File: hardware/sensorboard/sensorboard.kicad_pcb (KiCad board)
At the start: 2 copper layers, 51.7 x 19.3 mm, 23 parts, among them P1 PWR, P2 PROG, U1 ESP-07v2, U2 LMR16006Y, U3 BMP180_board, U4 DHT22

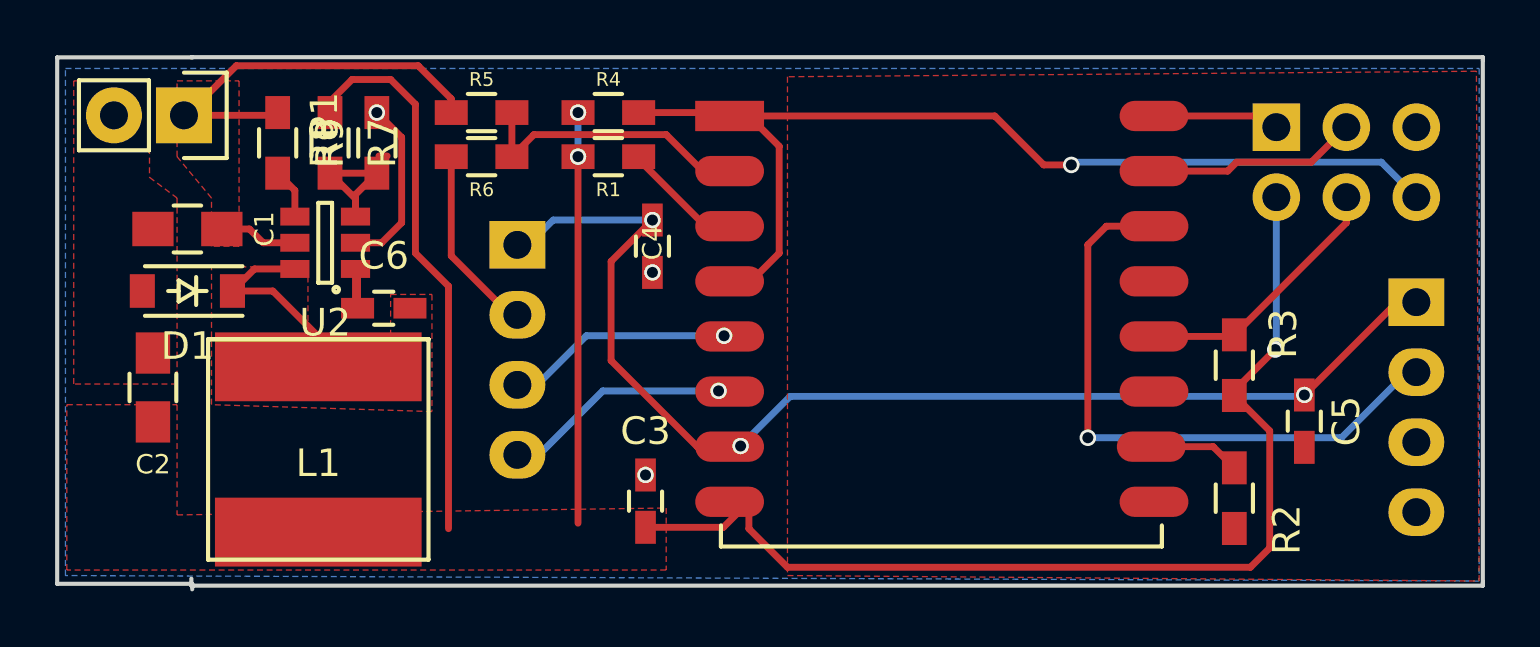
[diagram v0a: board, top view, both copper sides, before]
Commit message: Fix up silkscreening
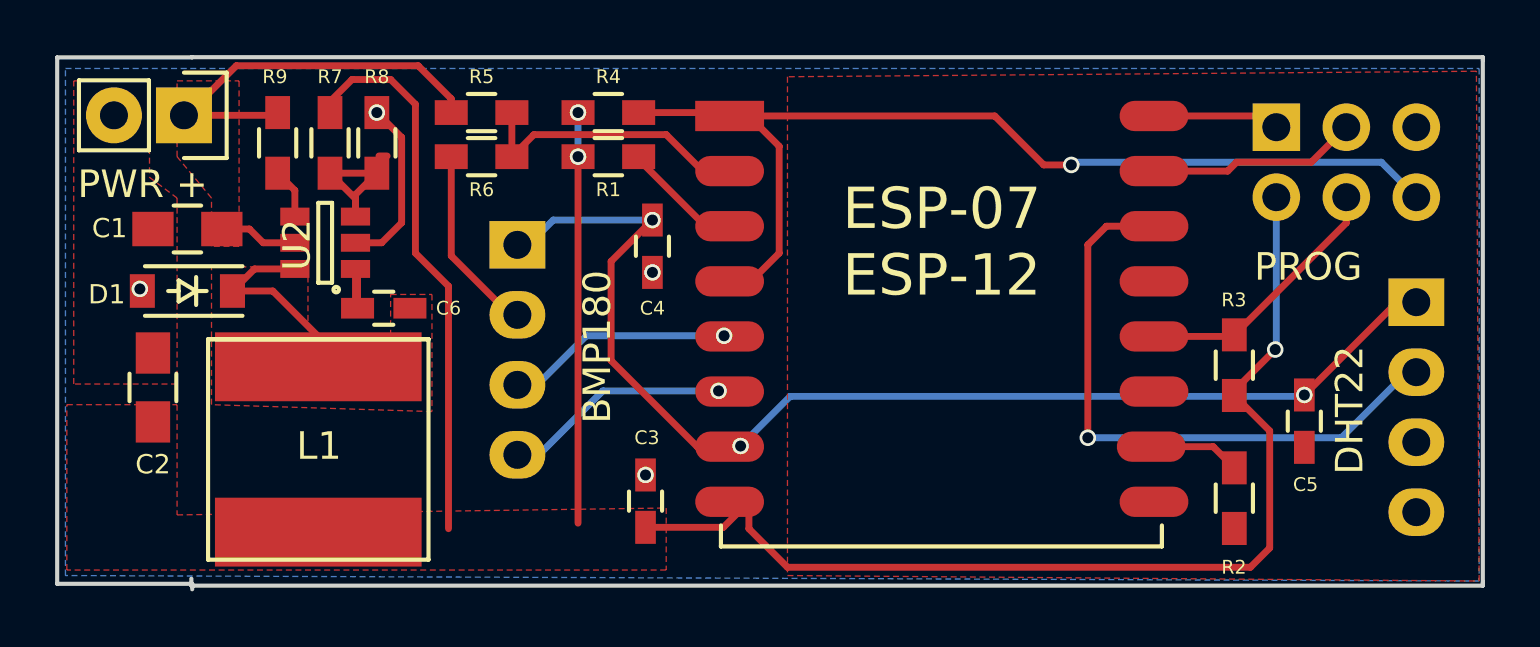
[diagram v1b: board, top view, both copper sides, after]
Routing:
- net GND: track 13.7 -> 13.8 mm, vias 3 -> 4
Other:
- board text added: "BMP180"
- board text added: "DATA"
- board text added: "DHT22"
- board text added: "ESP sensorboard v3.0"
- board text added: "ESP-07 ESP-12"
- board text added: "GND"
- board text added: "PROG"
- board text added: "PWR +"
- board text added: "SCL"
- board text added: "SDA"
- board text added: "VIN"
- board text added: "z2amiller"
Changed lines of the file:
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@@
     (area 123.324999 72.314999 175.208001 91.775001)
     (thickness 1.6)
-    (drawings 10)
-    (tracks 130)
+    (drawings 24)
+    (tracks 132)
     (zones 0)
     (modules 23)
@@
     (visible_elements FFFEFF7F)
     (pcbplotparams
-      (layerselection 0x010f0_80000001)
+      (layerselection 0x010f0_ffffffff)
       (usegerberextensions true)
       (excludeedgelayer true)
@@
     (tags "capacitor 0805")
     (attr smd)
-    (fp_text reference C1 (at -2.794 0 270) (layer F.SilkS)
+    (fp_text reference C1 (at 2.825 0.025 360) (layer F.SilkS)
       (effects (font (size 0.7 0.7) (thickness 0.1)))
     )
@@
     (attr smd)
     (fp_text reference C2 (at -2.794 0 180) (layer F.SilkS)
-      (effects (font (size 0.7 0.7) (thickness 0.15)))
+      (effects (font (size 0.7 0.7) (thickness 0.1)))
     )
     (fp_text value 10uf (at 0 2.1 90) (layer F.Fab)
@@
     (tags "resistor 0603")
     (attr smd)
-    (fp_text reference R4 (at 0 -1.2) (layer F.SilkS)
-      (effects (font (size 0.5 0.5) (thickness 0.125)))
+    (fp_text reference R4 (at 0 -1.3) (layer F.SilkS)
+      (effects (font (size 0.5 0.5) (thickness 0.1)))
     )
     (fp_text value 10k (at 0 1.9) (layer F.Fab)
@@
     (tags "resistor 0603")
     (attr smd)
-    (fp_text reference R3 (at 1.143 1.778 270) (layer F.SilkS)
-      (effects (font (size 1 1) (thickness 0.15)))
+    (fp_text reference R3 (at 2.366 -0.016 180) (layer F.SilkS)
+      (effects (font (size 0.5 0.5) (thickness 0.1)))
     )
     (fp_text value 10k (at 0 1.9 90) (layer F.Fab)
@@
     (tags "resistor 0603")
     (attr smd)
-    (fp_text reference R2 (at 1.143 -1.905 450) (layer F.SilkS)
-      (effects (font (size 1 1) (thickness 0.15)))
+    (fp_text reference R2 (at 2.508 0.016 360) (layer F.SilkS)
+      (effects (font (size 0.5 0.5) (thickness 0.1)))
     )
     (fp_text value 10k (at 0 1.9 270) (layer F.Fab)
@@
     (attr smd)
     (fp_text reference R1 (at 0 1.2) (layer F.SilkS)
-      (effects (font (size 0.5 0.5) (thickness 0.125)))
+      (effects (font (size 0.5 0.5) (thickness 0.1)))
     )
     (fp_text value 10k (at 0 1.9) (layer F.Fab)
@@
     (tags "capacitor 0603")
     (attr smd)
-    (fp_text reference C5 (at 0 1.524 90) (layer F.SilkS)
-      (effects (font (size 1 1) (thickness 0.15)))
+    (fp_text reference C5 (at -2.302 0.044 180) (layer F.SilkS)
+      (effects (font (size 0.5 0.5) (thickness 0.1)))
     )
     (fp_text value 100nf (at 0 1.9 90) (layer F.Fab)
@@
     (tags "capacitor 0603")
     (attr smd)
-    (fp_text reference C3 (at 2.54 0 180) (layer F.SilkS)
-      (effects (font (size 1 1) (thickness 0.15)))
+    (fp_text reference C3 (at 2.3 0.05 180) (layer F.SilkS)
+      (effects (font (size 0.5 0.5) (thickness 0.1)))
     )
     (fp_text value 100nf (at 0 1.9 90) (layer F.Fab)
@@
     (tags "capacitor 0603")
     (attr smd)
-    (fp_text reference C4 (at 0.127 0 90) (layer F.SilkS)
-      (effects (font (size 0.7 0.7) (thickness 0.15)))
+    (fp_text reference C4 (at -2.25 0 180) (layer F.SilkS)
+      (effects (font (size 0.5 0.5) (thickness 0.1)))
     )
     (fp_text value 100nf (at 0 1.9 90) (layer F.Fab)
@@
     (tags "resistor 0603")
     (attr smd)
-    (fp_text reference R5 (at 0 -1.2) (layer F.SilkS)
-      (effects (font (size 0.5 0.5) (thickness 0.125)))
+    (fp_text reference R5 (at 0 -1.3) (layer F.SilkS)
+      (effects (font (size 0.5 0.5) (thickness 0.1)))
     )
     (fp_text value 470K (at 0 1.9) (layer F.Fab)
@@
     (attr smd)
     (fp_text reference R6 (at 0 -1.2 180) (layer F.SilkS)
-      (effects (font (size 0.5 0.5) (thickness 0.125)))
+      (effects (font (size 0.5 0.5) (thickness 0.1)))
     )
     (fp_text value 47K (at 0 1.9 180) (layer F.Fab)
@@
     (tags "capacitor 0603")
     (attr smd)
-    (fp_text reference C6 (at 0 -1.9) (layer F.SilkS)
-      (effects (font (size 1 1) (thickness 0.15)))
+    (fp_text reference C6 (at 2.35 0) (layer F.SilkS)
+      (effects (font (size 0.5 0.5) (thickness 0.1)))
     )
     (fp_text value 1uf (at 0 1.9) (layer F.Fab)
@@
     (tags SOD-123)
     (attr smd)
-    (fp_text reference D1 (at 0 -2 180) (layer F.SilkS)
-      (effects (font (size 1 1) (thickness 0.15)))
+    (fp_text reference D1 (at 2.925 -0.125 180) (layer F.SilkS)
+      (effects (font (size 0.7 0.7) (thickness 0.1)))
     )
     (fp_text value "60V 1A" (at 0 2.1 180) (layer F.Fab)
@@
   (module Inductors:NR8040_HandSoldering (layer F.Cu)
     (at 132.875 86.625)
-    (fp_text reference L1 (at 0 0.5) (layer F.SilkS)
+    (fp_text reference L1 (at 0.025 -0.125) (layer F.SilkS)
       (effects (font (size 1 1) (thickness 0.15)))
     )
@@
     (descr "Through hole pin header")
     (tags "pin header")
-    (fp_text reference P1 (at 0 -5.1 270) (layer F.SilkS)
+    (fp_text reference P1 (at 2.5 2.5 360) (layer F.SilkS) hide
       (effects (font (size 1 1) (thickness 0.15)))
     )
@@
     (tags "resistor 0603")
     (attr smd)
-    (fp_text reference R7 (at 0 -1.9 270) (layer F.SilkS)
-      (effects (font (size 1 1) (thickness 0.15)))
+    (fp_text reference R7 (at -2.4 0 360) (layer F.SilkS)
+      (effects (font (size 0.5 0.5) (thickness 0.1)))
     )
     (fp_text value 33k (at 0 1.9 270) (layer F.Fab)
@@
     (tags "resistor 0603")
     (attr smd)
-    (fp_text reference R8 (at 0 -1.9 90) (layer F.SilkS)
-      (effects (font (size 1 1) (thickness 0.15)))
+    (fp_text reference R8 (at 2.4 0 180) (layer F.SilkS)
+      (effects (font (size 0.5 0.5) (thickness 0.1)))
     )
     (fp_text value 10k (at 0 1.9 90) (layer F.Fab)
@@
     (tags "resistor 0603")
     (attr smd)
-    (fp_text reference R9 (at 0 -1.9 270) (layer F.SilkS)
-      (effects (font (size 1 1) (thickness 0.15)))
+    (fp_text reference R9 (at -2.4 0.1 360) (layer F.SilkS)
+      (effects (font (size 0.5 0.5) (thickness 0.1)))
     )
     (fp_text value 100k (at 0 1.9 270) (layer F.Fab)
@@
     (tags SOT-23-6)
     (attr smd)
-    (fp_text reference U2 (at 0 -2.9 180) (layer F.SilkS)
+    (fp_text reference U2 (at 1.025 -0.075 450) (layer F.SilkS)
       (effects (font (size 1 1) (thickness 0.15)))
     )
@@
       (rotate (xyz 0 0 0))
     )
+  )
+  (gr_text SDA (at 143 86.8) (layer B.SilkS)
+    (effects (font (size 0.7 0.7) (thickness 0.15)) (justify mirror))
+  )
+  (gr_text SCL (at 142.9 84.3) (layer B.SilkS)
+    (effects (font (size 0.7 0.7) (thickness 0.15)) (justify mirror))
+  )
+  (gr_text VIN (at 142.8 79.2) (layer B.SilkS)
+    (effects (font (size 0.7 0.7) (thickness 0.15)) (justify mirror))
+  )
+  (gr_text GND (at 142.9 81.8) (layer B.SilkS)
+    (effects (font (size 0.7 0.7) (thickness 0.15)) (justify mirror))
+  )
+  (gr_text GND (at 169.9 89) (layer B.SilkS)
+    (effects (font (size 0.7 0.7) (thickness 0.15)) (justify mirror))
+  )
+  (gr_text DATA (at 169.7 83.8) (layer B.SilkS)
+    (effects (font (size 0.7 0.7) (thickness 0.15)) (justify mirror))
+  )
+  (gr_text VIN (at 169.9 81.4) (layer B.SilkS)
+    (effects (font (size 0.7 0.7) (thickness 0.15)) (justify mirror))
+  )
+  (gr_text "ESP sensorboard v3.0" (at 149.6 74.1) (layer B.SilkS)
+    (effects (font (size 1.5 1.5) (thickness 0.3)) (justify mirror))
+  )
+  (gr_text z2amiller (at 155.8 90.3) (layer B.SilkS)
+    (effects (font (size 1 1) (thickness 0.2)) (justify mirror))
+  )
+  (gr_text BMP180 (at 143 82.9 90) (layer F.SilkS)
+    (effects (font (size 1 1) (thickness 0.2)))
+  )
+  (gr_text DHT22 (at 170.3 85.2 90) (layer F.SilkS)
+    (effects (font (size 1 1) (thickness 0.2)))
+  )
+  (gr_text PROG (at 168.8 80) (layer F.SilkS)
+    (effects (font (size 1 1) (thickness 0.25)))
+  )
+  (gr_text "ESP-07\nESP-12" (at 155.5 79.1) (layer F.SilkS)
+    (effects (font (size 1.5 1.5) (thickness 0.3)))
+  )
+  (gr_text "PWR +" (at 126.5 77) (layer F.SilkS)
+    (effects (font (size 1 1) (thickness 0.25)))
   )
   (gr_line (start 128.3 91.5) (end 128.3 91.7) (angle 90) (layer Edge.Cuts) (width 0.15))
@@
   (segment (start 130.375 78.625) (end 130.875 79.125) (width 0.25) (layer F.Cu) (net 1))
   (segment (start 128 74.5) (end 128.5 74.5) (width 0.25) (layer F.Cu) (net 1))
+  (via (at 126.4 80.8) (size 0.6) (drill 0.4) (layers F.Cu B.Cu) (net 2) (status 800000))
+  (segment (start 126.4 80.8) (end 126.49 80.875) (width 0.25) (layer F.Cu) (net 2) (status C00000))
   (via (at 144.75 87.55) (size 0.6) (drill 0.4) (layers F.Cu B.Cu) (net 2))
   (segment (start 144.75 87.55) (end 144.7 87.6) (width 0.25) (layer B.Cu) (net 2))

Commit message: Fix up the bottom edge cuts
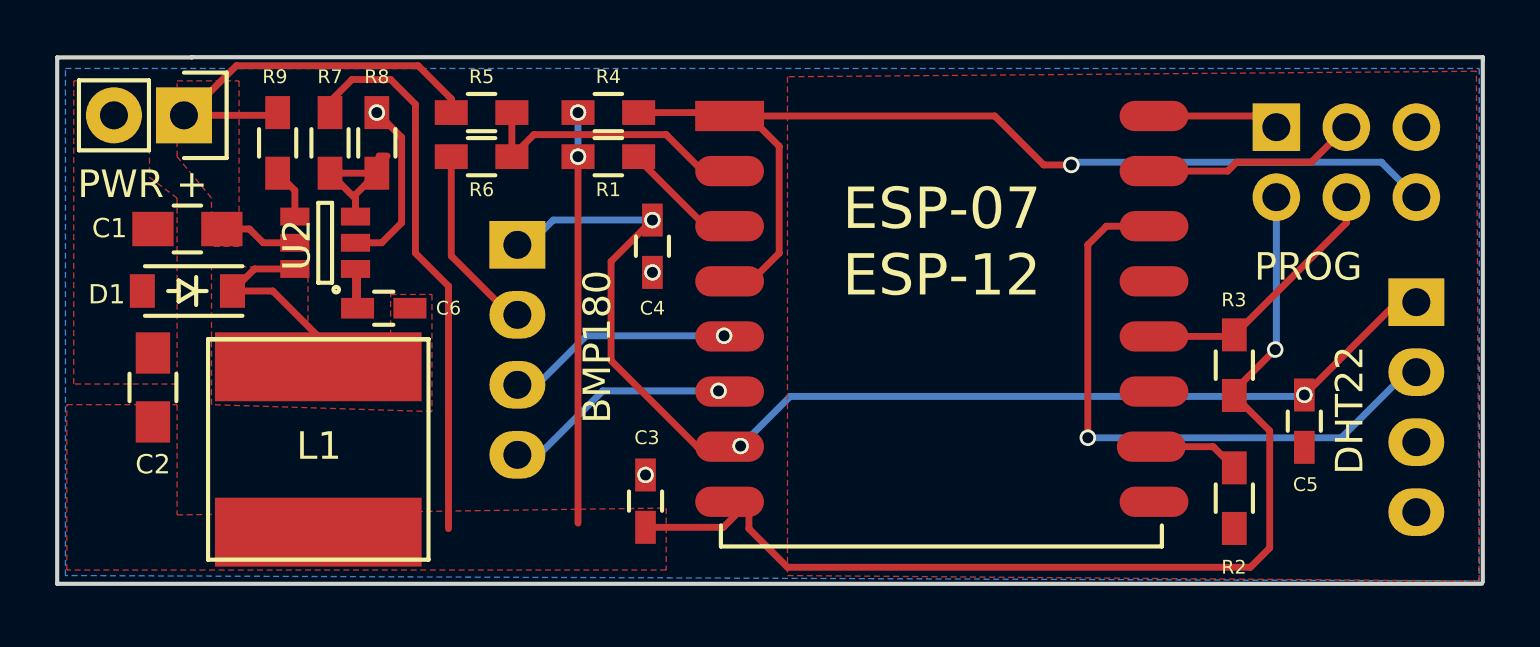
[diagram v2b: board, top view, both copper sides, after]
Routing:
- net GND: track 13.8 -> 13.7 mm, vias 4 -> 3
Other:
- board size 51.7 x 19.3 mm -> 51.7 x 19.1 mm
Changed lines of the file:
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@@
     (area 123.324999 72.314999 175.208001 91.775001)
     (thickness 1.6)
-    (drawings 24)
-    (tracks 132)
+    (drawings 20)
+    (tracks 130)
     (zones 0)
     (modules 23)
@@
     )
   )
+  (gr_line (start 175.133 72.517) (end 175.133 91.44) (angle 90) (layer Edge.Cuts) (width 0.15))
+  (gr_line (start 123.4 91.5) (end 175.1 91.5) (angle 90) (layer Edge.Cuts) (width 0.15))
   (gr_text SDA (at 143 86.8) (layer B.SilkS)
     (effects (font (size 0.7 0.7) (thickness 0.15)) (justify mirror))
@@
     (effects (font (size 1 1) (thickness 0.25)))
   )
-  (gr_line (start 128.3 91.5) (end 128.3 91.7) (angle 90) (layer Edge.Cuts) (width 0.15))
-  (gr_line (start 123.4 91.5) (end 128.3 91.5) (angle 90) (layer Edge.Cuts) (width 0.15))
   (gr_line (start 123.4 72.4) (end 123.4 91.5) (angle 90) (layer Edge.Cuts) (width 0.15))
   (gr_line (start 128.3 72.4) (end 123.4 72.4) (angle 90) (layer Edge.Cuts) (width 0.15))
   (gr_line (start 175.133 72.39) (end 175.133 72.517) (angle 90) (layer Edge.Cuts) (width 0.15))
   (gr_line (start 128.27 72.39) (end 175.133 72.39) (angle 90) (layer Edge.Cuts) (width 0.15))
-  (gr_line (start 128.27 91.567) (end 128.27 91.313) (angle 90) (layer Edge.Cuts) (width 0.15))
-  (gr_line (start 175.133 91.567) (end 175.133 91.44) (angle 90) (layer Edge.Cuts) (width 0.15))
-  (gr_line (start 128.27 91.567) (end 175.133 91.567) (angle 90) (layer Edge.Cuts) (width 0.15))
-  (gr_line (start 175.133 72.517) (end 175.133 91.44) (angle 90) (layer Edge.Cuts) (width 0.15))
   (segment (start 135.075 75.975) (end 135.375 75.975) (width 0.25) (layer F.Cu) (net 0))
   (segment (start 128 74.5) (end 131.3 74.5) (width 0.25) (layer F.Cu) (net 1))
@@
   (segment (start 130.375 78.625) (end 130.875 79.125) (width 0.25) (layer F.Cu) (net 1))
   (segment (start 128 74.5) (end 128.5 74.5) (width 0.25) (layer F.Cu) (net 1))
-  (via (at 126.4 80.8) (size 0.6) (drill 0.4) (layers F.Cu B.Cu) (net 2) (status 800000))
-  (segment (start 126.4 80.8) (end 126.49 80.875) (width 0.25) (layer F.Cu) (net 2) (status C00000))
   (via (at 144.75 87.55) (size 0.6) (drill 0.4) (layers F.Cu B.Cu) (net 2))
   (segment (start 144.75 87.55) (end 144.7 87.6) (width 0.25) (layer B.Cu) (net 2))
@@
   (segment (start 135.175 79.125) (end 135.9 78.4) (width 0.25) (layer F.Cu) (net 2))
   (segment (start 134.225 79.125) (end 134.625 79.125) (width 0.25) (layer F.Cu) (net 2))
-  (segment (start 166.116 84.666) (end 166.116 84.484) (width 0.25) (layer F.Cu) (net 3) (status C00000))
-  (segment (start 166.116 84.484) (end 167.6 83) (width 0.25) (layer F.Cu) (net 3) (status 400000))
-  (segment (start 167.64 82.96) (end 167.64 77.47) (width 0.25) (layer B.Cu) (net 3) (status 800000))
+  (segment (start 166.116 84.666) (end 166.116 84.484) (width 0.25) (layer F.Cu) (net 3))
+  (segment (start 166.116 84.484) (end 167.6 83) (width 0.25) (layer F.Cu) (net 3))
+  (segment (start 167.64 82.96) (end 167.64 77.47) (width 0.25) (layer B.Cu) (net 3))
   (segment (start 167.6 83) (end 167.64 82.96) (width 0.25) (layer B.Cu) (net 3))
   (via (at 167.6 83) (size 0.6) (drill 0.4) (layers F.Cu B.Cu) (net 3))
-  (segment (start 148.5011 88.5236) (end 148.5011 89.5011) (width 0.25) (layer F.Cu) (net 3) (status 400000))
-  (segment (start 167.4 85.95) (end 166.116 84.666) (width 0.25) (layer F.Cu) (net 3) (status 800000))
+  (segment (start 148.5011 88.5236) (end 148.5011 89.5011) (width 0.25) (layer F.Cu) (net 3))
+  (segment (start 167.4 85.95) (end 166.116 84.666) (width 0.25) (layer F.Cu) (net 3))
   (segment (start 167.4 90.2) (end 167.4 85.95) (width 0.25) (layer F.Cu) (net 3))
   (segment (start 166.7 90.9) (end 167.4 90.2) (width 0.25) (layer F.Cu) (net 3))
@@
   (segment (start 144.75 89.45) (end 147.5747 89.45) (width 0.25) (layer F.Cu) (net 3))
   (segment (start 147.5747 89.45) (end 148.5011 88.5236) (width 0.25) (layer F.Cu) (net 3))
-  (via (at 168.656 84.648) (size 0.6) (drill 0.4) (layers F.Cu B.Cu) (net 4) (status C00000))
+  (via (at 168.656 84.648) (size 0.6) (drill 0.4) (layers F.Cu B.Cu) (net 4))
   (segment (start 172.024 81.28) (end 168.656 84.648) (width 0.25) (layer F.Cu) (net 4))
-  (segment (start 148.2 86.5) (end 148.2236 86.5236) (width 0.25) (layer F.Cu) (net 4) (status C00000))
-  (via (at 148.2 86.5) (size 0.6) (drill 0.4) (layers F.Cu B.Cu) (net 4) (status 800000))
+  (segment (start 148.2 86.5) (end 148.2236 86.5236) (width 0.25) (layer F.Cu) (net 4))
+  (via (at 148.2 86.5) (size 0.6) (drill 0.4) (layers F.Cu B.Cu) (net 4))
   (segment (start 150 84.7) (end 148.2 86.5) (width 0.25) (layer B.Cu) (net 4))
   (segment (start 168.604 84.7) (end 150 84.7) (width 0.25) (layer B.Cu) (net 4))
-  (segment (start 168.656 84.648) (end 168.604 84.7) (width 0.25) (layer B.Cu) (net 4) (status 400000))
-  (segment (start 148.2236 86.5236) (end 148.5011 86.5236) (width 0.25) (layer F.Cu) (net 4) (status C00000))
+  (segment (start 168.656 84.648) (end 168.604 84.7) (width 0.25) (layer B.Cu) (net 4))
+  (segment (start 148.2236 86.5236) (end 148.5011 86.5236) (width 0.25) (layer F.Cu) (net 4))
   (segment (start 172.72 81.28) (end 172.024 81.28) (width 0.25) (layer F.Cu) (net 4))
   (segment (start 148.5011 86.5236) (end 146.6236 86.5236) (width 0.25) (layer F.Cu) (net 4))
@@
   (via (at 147.4 84.5) (size 0.6) (drill 0.4) (layers F.Cu B.Cu) (net 12))
   (segment (start 147.4 84.5) (end 148.5011 84.5236) (width 0.25) (layer F.Cu) (net 12))
-  (segment (start 172.72 83.82) (end 172.38 83.82) (width 0.25) (layer B.Cu) (net 15) (status C00000))
-  (segment (start 172.38 83.82) (end 170 86.2) (width 0.25) (layer B.Cu) (net 15) (status 400000))
+  (segment (start 172.72 83.82) (end 172.38 83.82) (width 0.25) (layer B.Cu) (net 15))
+  (segment (start 172.38 83.82) (end 170 86.2) (width 0.25) (layer B.Cu) (net 15))
   (segment (start 170 86.2) (end 160.8 86.2) (width 0.25) (layer B.Cu) (net 15))
   (via (at 160.8 86.2) (size 0.6) (drill 0.4) (layers F.Cu B.Cu) (net 15))
   (segment (start 160.8 86.2) (end 160.8 79.2) (width 0.25) (layer F.Cu) (net 15))
   (segment (start 160.8 79.2) (end 161.4764 78.5236) (width 0.25) (layer F.Cu) (net 15))
-  (segment (start 161.4764 78.5236) (end 162.5011 78.5236) (width 0.25) (layer F.Cu) (net 15) (status 800000))
+  (segment (start 161.4764 78.5236) (end 162.5011 78.5236) (width 0.25) (layer F.Cu) (net 15))
   (segment (start 148.5011 76.5236) (end 146.8236 76.5236) (width 0.25) (layer F.Cu) (net 17))
   (segment (start 146.8236 76.5236) (end 145.5 75.2) (width 0.25) (layer F.Cu) (net 17))
